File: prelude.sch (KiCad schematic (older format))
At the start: 1 part

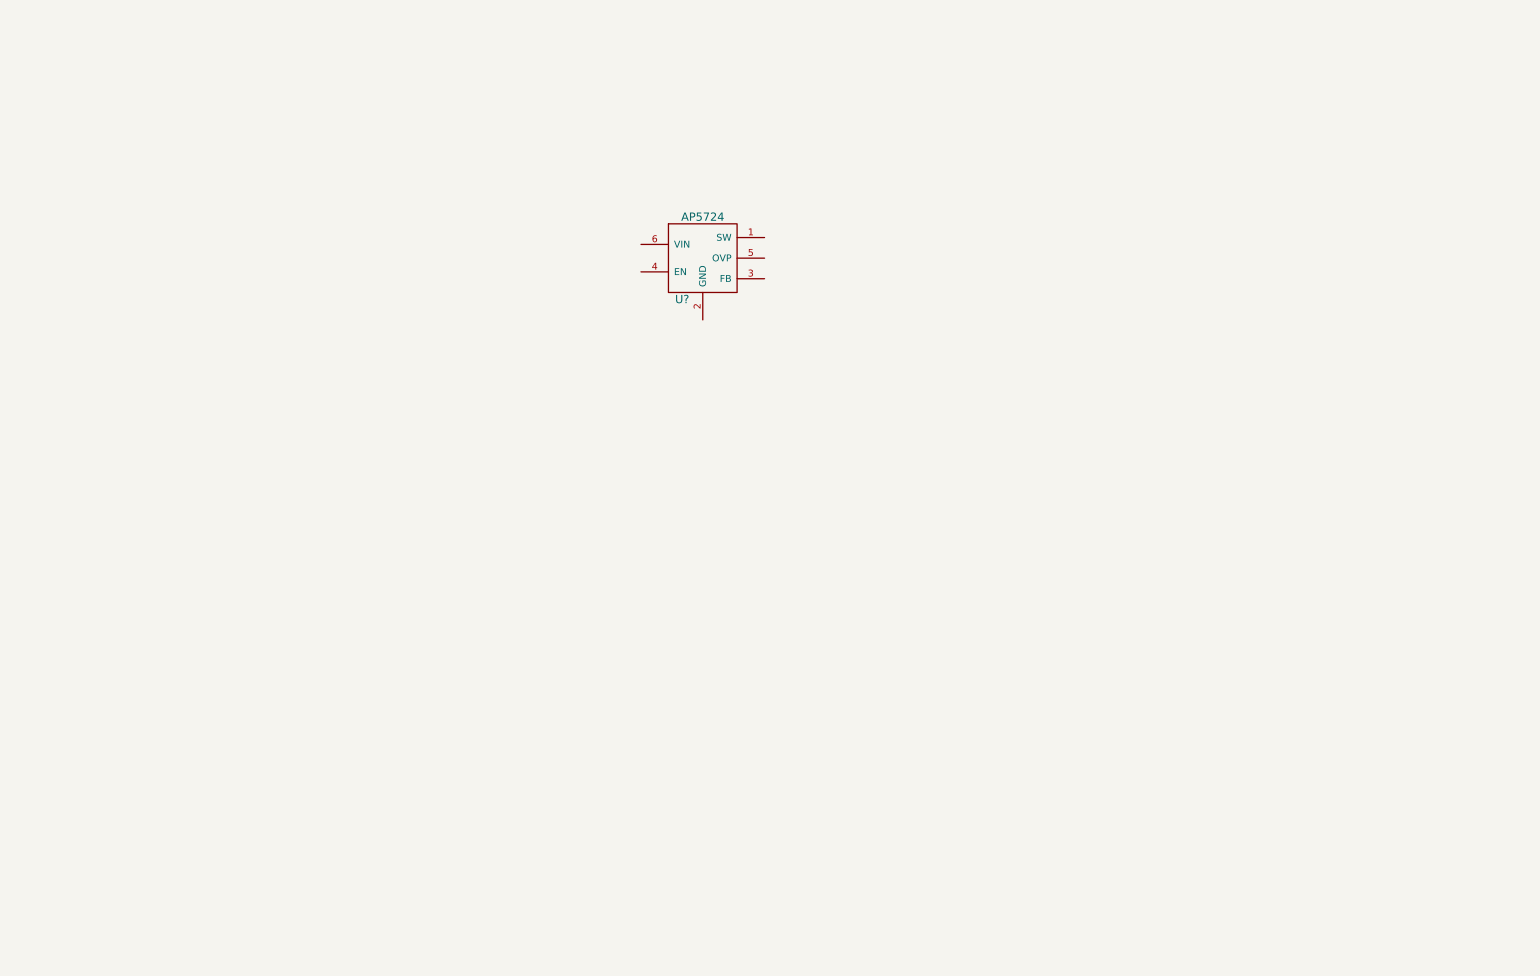
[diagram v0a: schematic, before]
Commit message: Adds MCU and 50 pin connector to schematic
Adds STM32F103RETx to schematic
Adds STM32 library to project
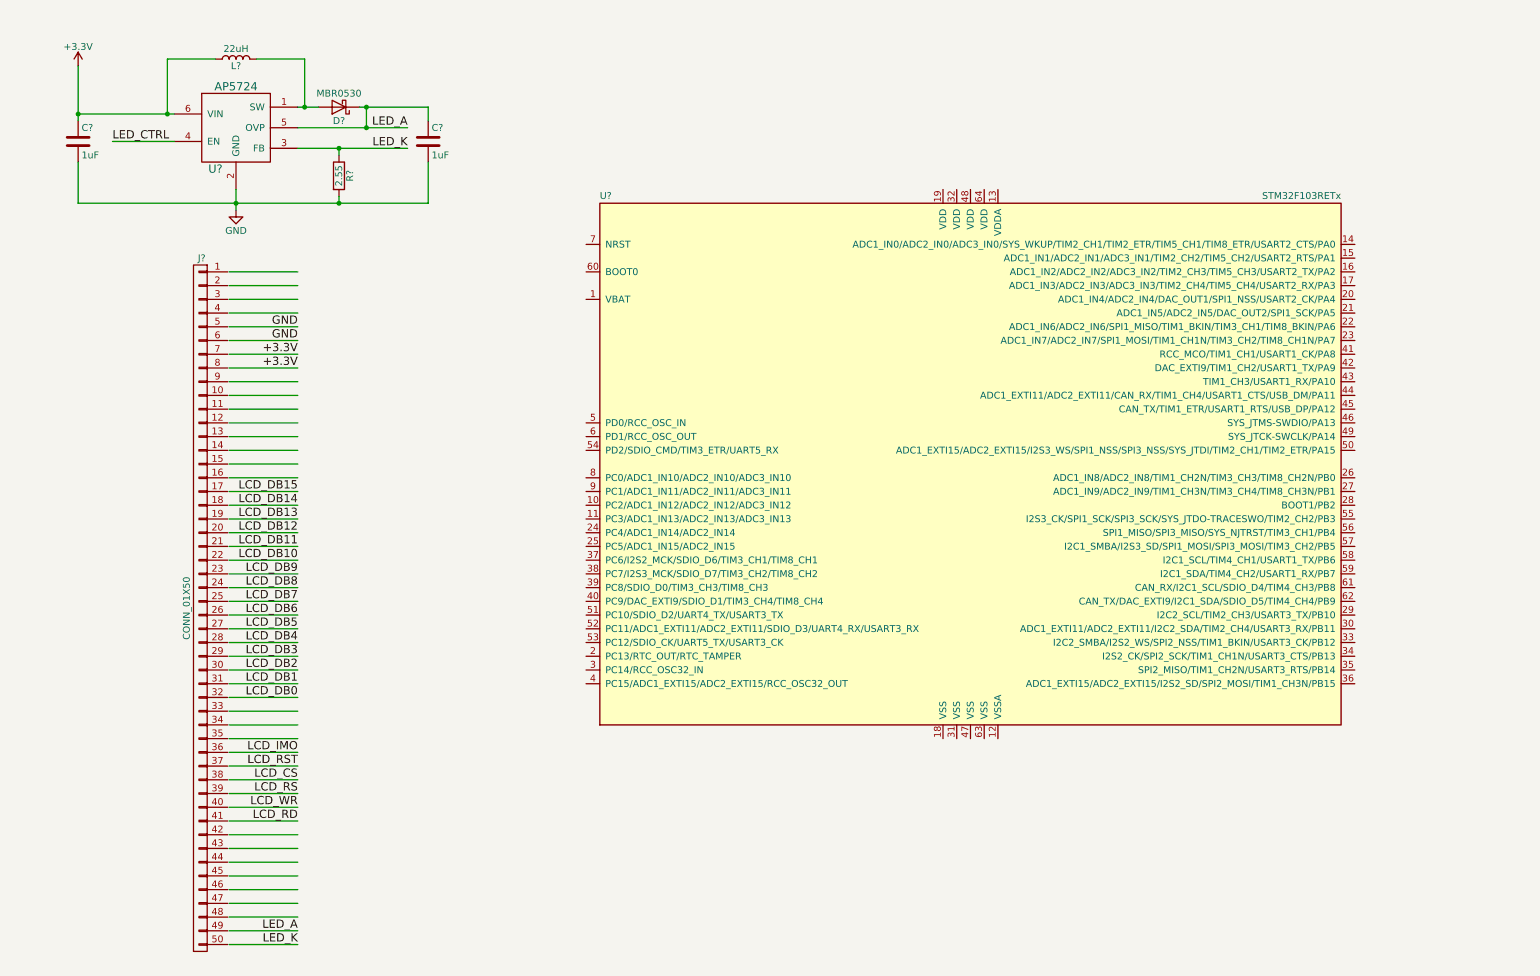
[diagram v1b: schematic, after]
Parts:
- added C? (x2): 1uF, symbol C
- added D?: MBR0530, symbol D_Schottky
- added J?: CONN_01X50, symbol CONN_01X50
- added L?: 22uH, symbol L
- added R?: 2.55, symbol R
- added U?: STM32F103RETx, LQFP64, symbol STM32F103RETx
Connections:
- net labels added: +3.3V, GND, LCD_CS, LCD_DB0, LCD_DB1, LCD_DB10, LCD_DB11, LCD_DB12, LCD_DB13, LCD_DB14, LCD_DB15, LCD_DB2, LCD_DB3, LCD_DB4, LCD_DB5, LCD_DB6, LCD_DB7, LCD_DB8, LCD_DB9, LCD_IMO, LCD_RD, LCD_RS, LCD_RST, LCD_WR, LED_A, LED_CTRL, LED_K
- wire segments 0 -> 69
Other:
- moved on the sheet: U?

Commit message: Adds main 3.3 power supply based on LM3671MF
Removed and added back 50-in connector, after fixing grid alignment
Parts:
- removed J?: CONN_01X50, symbol CONN_01X50
- added C?: 10uF, symbol C
- added C?: C, symbol C
- added D?: LED, symbol LED
- added F?: Polyfuse, symbol Polyfuse
- added J?: USB_OTG, symbol USB_OTG
- added J?: CONN_01X50, symbol CONN_01X50
- added L?: L, symbol L
- added R?: 330, symbol R
- added U?: LM3671MF-3.3, SOT95P284X122-5N, symbol LM3671MF-3.3
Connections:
- net labels added: +3V3, VCC
- wire segments 69 -> 84
- no-connect marks 0 -> 22
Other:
- moved on the sheet: C?, D?, L?, R?, U?

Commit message: Updates USB connector to to USB C
Added necessary connections and resistors (5.1K pulldown) to allow for device enumeration
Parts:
- removed J?: USB_OTG, symbol USB_OTG
- added J?: USB_C, symbol USB_C
- added R? (x2): 5K1, symbol R
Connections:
- net labels added: D+, D-, VBUS
- wire segments 84 -> 98
- no-connect marks 22 -> 32
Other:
- moved on the sheet: C?, D?, F?, L?, R?, U?

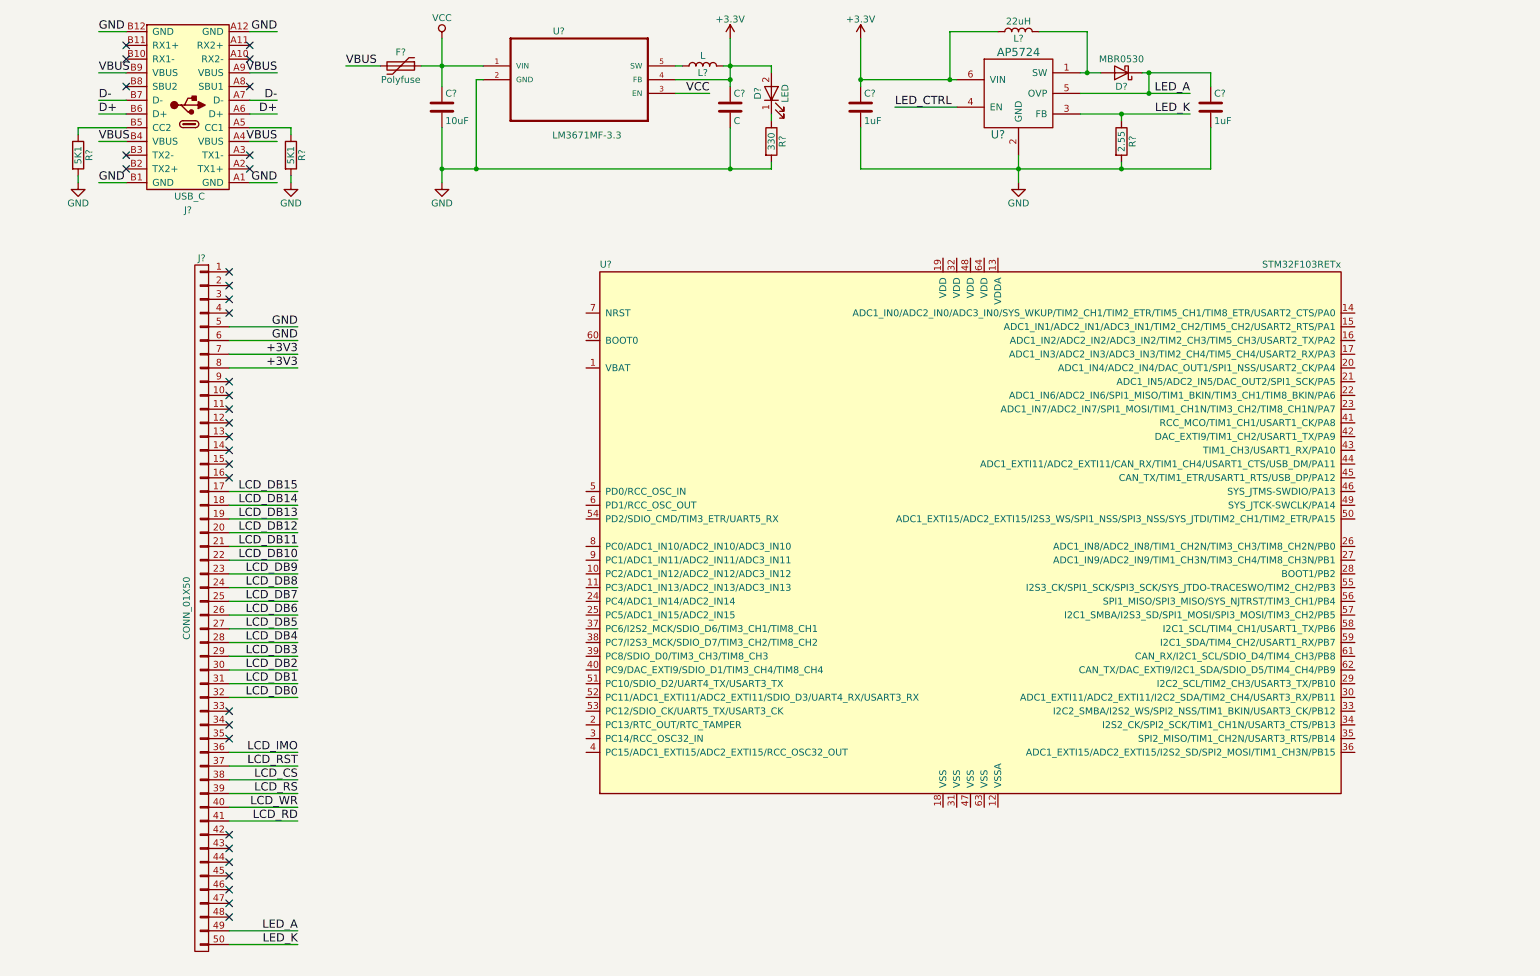
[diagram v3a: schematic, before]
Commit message: Updates schematic and project
Adds passives and wires to MCU
Adds switches library to project
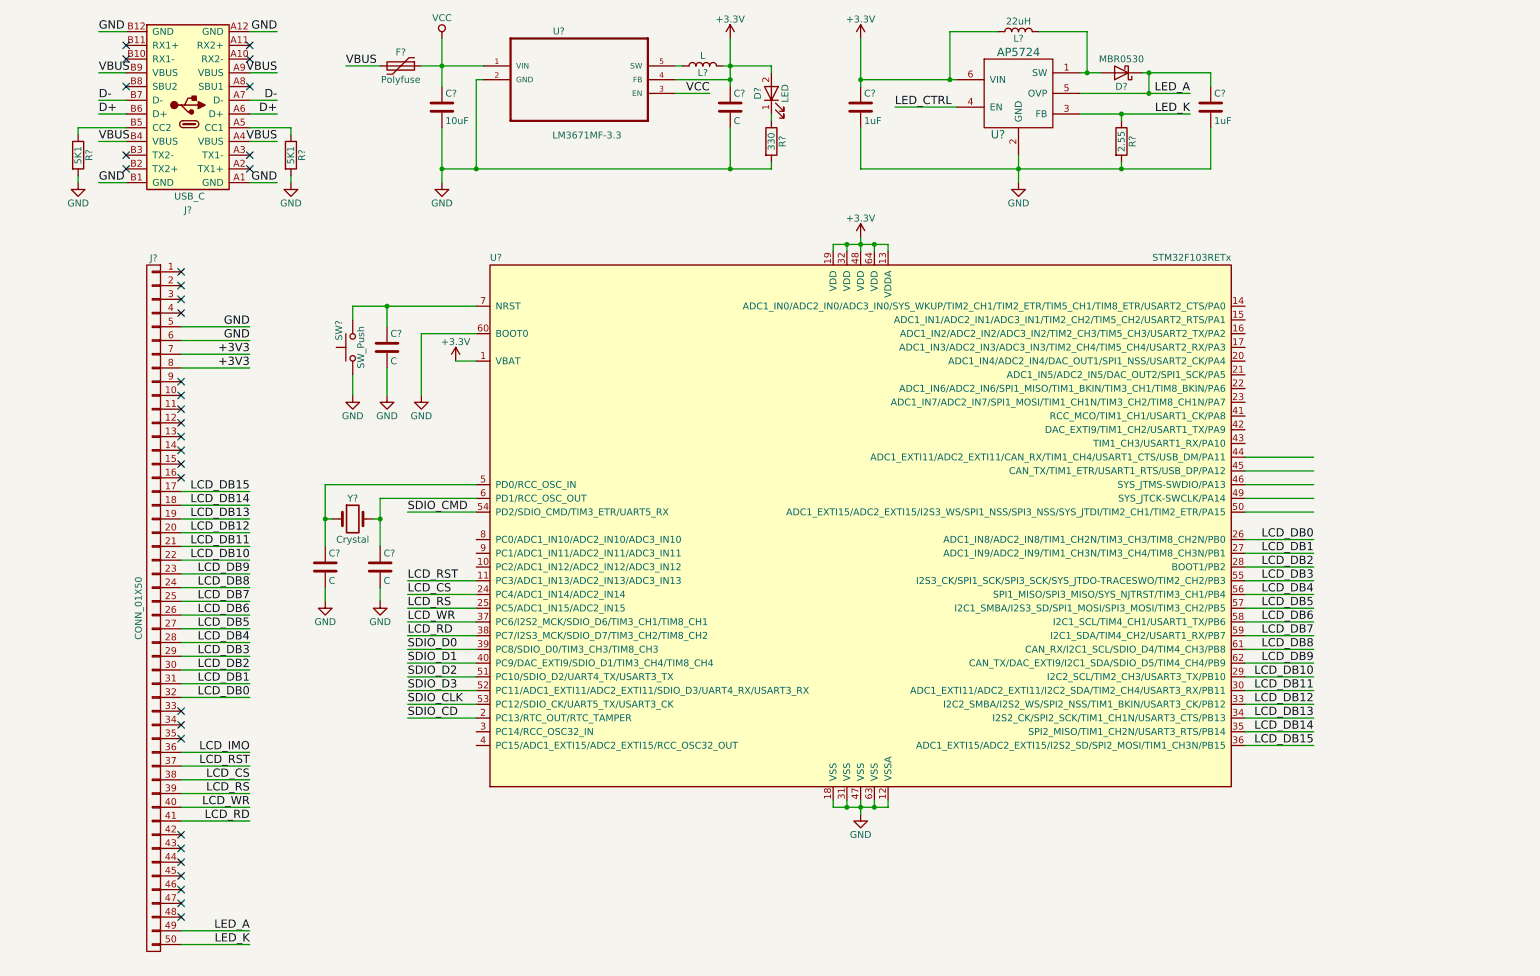
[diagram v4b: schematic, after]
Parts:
- added C? (x3): C, symbol C
- added SW?: SW_Push, symbol SW_Push
- added Y?: Crystal, symbol Crystal
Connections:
- net +3V3: now also U?.1 (VBAT), U?.13 (VDDA), U?.19 (VDD), U?.32 (VDD), U?.48 (VDD), U?.64 (VDD)
- net GND: now also U?.12 (VSSA), U?.18 (VSS), U?.31 (VSS), U?.47 (VSS), U?.60 (BOOT0), U?.63 (VSS), C?.2, C?.2, C?.2, SW?.1
- net LCD_CS: now also U?.24 (PC4/ADC1_IN14/ADC2_IN14)
- net LCD_DB0: now also U?.26 (ADC1_IN8/ADC2_IN8/TIM1_CH2N/TIM3_CH3/TIM8_CH2N/PB0)
- net LCD_DB1: now also U?.27 (ADC1_IN9/ADC2_IN9/TIM1_CH3N/TIM3_CH4/TIM8_CH3N/PB1)
- net LCD_DB10: now also U?.29 (I2C2_SCL/TIM2_CH3/USART3_TX/PB10)
- net LCD_DB11: now also U?.30 (ADC1_EXTI11/ADC2_EXTI11/I2C2_SDA/TIM2_CH4/USART3_RX/PB11)
- net LCD_DB12: now also U?.33 (I2C2_SMBA/I2S2_WS/SPI2_NSS/TIM1_BKIN/USART3_CK/PB12)
- net LCD_DB13: now also U?.34 (I2S2_CK/SPI2_SCK/TIM1_CH1N/USART3_CTS/PB13)
- net LCD_DB14: now also U?.35 (SPI2_MISO/TIM1_CH2N/USART3_RTS/PB14)
- net LCD_DB15: now also U?.36 (ADC1_EXTI15/ADC2_EXTI15/I2S2_SD/SPI2_MOSI/TIM1_CH3N/PB15)
- net LCD_DB2: now also U?.28 (BOOT1/PB2)
- net LCD_DB3: now also U?.55 (I2S3_CK/SPI1_SCK/SPI3_SCK/SYS_JTDO-TRACESWO/TIM2_CH2/PB3)
- net LCD_DB4: now also U?.56 (SPI1_MISO/SPI3_MISO/SYS_NJTRST/TIM3_CH1/PB4)
- net LCD_DB5: now also U?.57 (I2C1_SMBA/I2S3_SD/SPI1_MOSI/SPI3_MOSI/TIM3_CH2/PB5)
- net LCD_DB6: now also U?.58 (I2C1_SCL/TIM4_CH1/USART1_TX/PB6)
- net LCD_DB7: now also U?.59 (I2C1_SDA/TIM4_CH2/USART1_RX/PB7)
- net LCD_DB8: now also U?.61 (CAN_RX/I2C1_SCL/SDIO_D4/TIM4_CH3/PB8)
- net LCD_DB9: now also U?.62 (CAN_TX/DAC_EXTI9/I2C1_SDA/SDIO_D5/TIM4_CH4/PB9)
- net LCD_RD: now also U?.38 (PC7/I2S3_MCK/SDIO_D7/TIM3_CH2/TIM8_CH2)
- net LCD_RS: now also U?.25 (PC5/ADC1_IN15/ADC2_IN15)
- net LCD_RST: now also U?.11 (PC3/ADC1_IN13/ADC2_IN13/ADC3_IN13)
- net LCD_WR: now also U?.37 (PC6/I2S2_MCK/SDIO_D6/TIM3_CH1/TIM8_CH1)
- net SDIO_CD: now reaches U?.2 (PC13/RTC_OUT/RTC_TAMPER)
- net SDIO_D0: now reaches U?.39 (PC8/SDIO_D0/TIM3_CH3/TIM8_CH3)
- net SDIO_D1: now reaches U?.40 (PC9/DAC_EXTI9/SDIO_D1/TIM3_CH4/TIM8_CH4)
- net at U?.5 (PD0/RCC_OSC_IN): now also C?.1, Y?.1
- net SDIO_D2: now reaches U?.51 (PC10/SDIO_D2/UART4_TX/USART3_TX)
- net SDIO_D3: now reaches U?.52 (PC11/ADC1_EXTI11/ADC2_EXTI11/SDIO_D3/UART4_RX/USART3_RX)
- net SDIO_CLK: now reaches U?.53 (PC12/SDIO_CK/UART5_TX/USART3_CK)
- net SDIO_CMD: now reaches U?.54 (PD2/SDIO_CMD/TIM3_ETR/UART5_RX)
- net at U?.6 (PD1/RCC_OSC_OUT): now also C?.1, Y?.2
- net at U?.7 (NRST): now also C?.1, SW?.2
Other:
- moved on the sheet: J?, U?

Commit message: Several updates to schematic
Adds decoupling capacitors
Adds debug connector
Adds values to several components
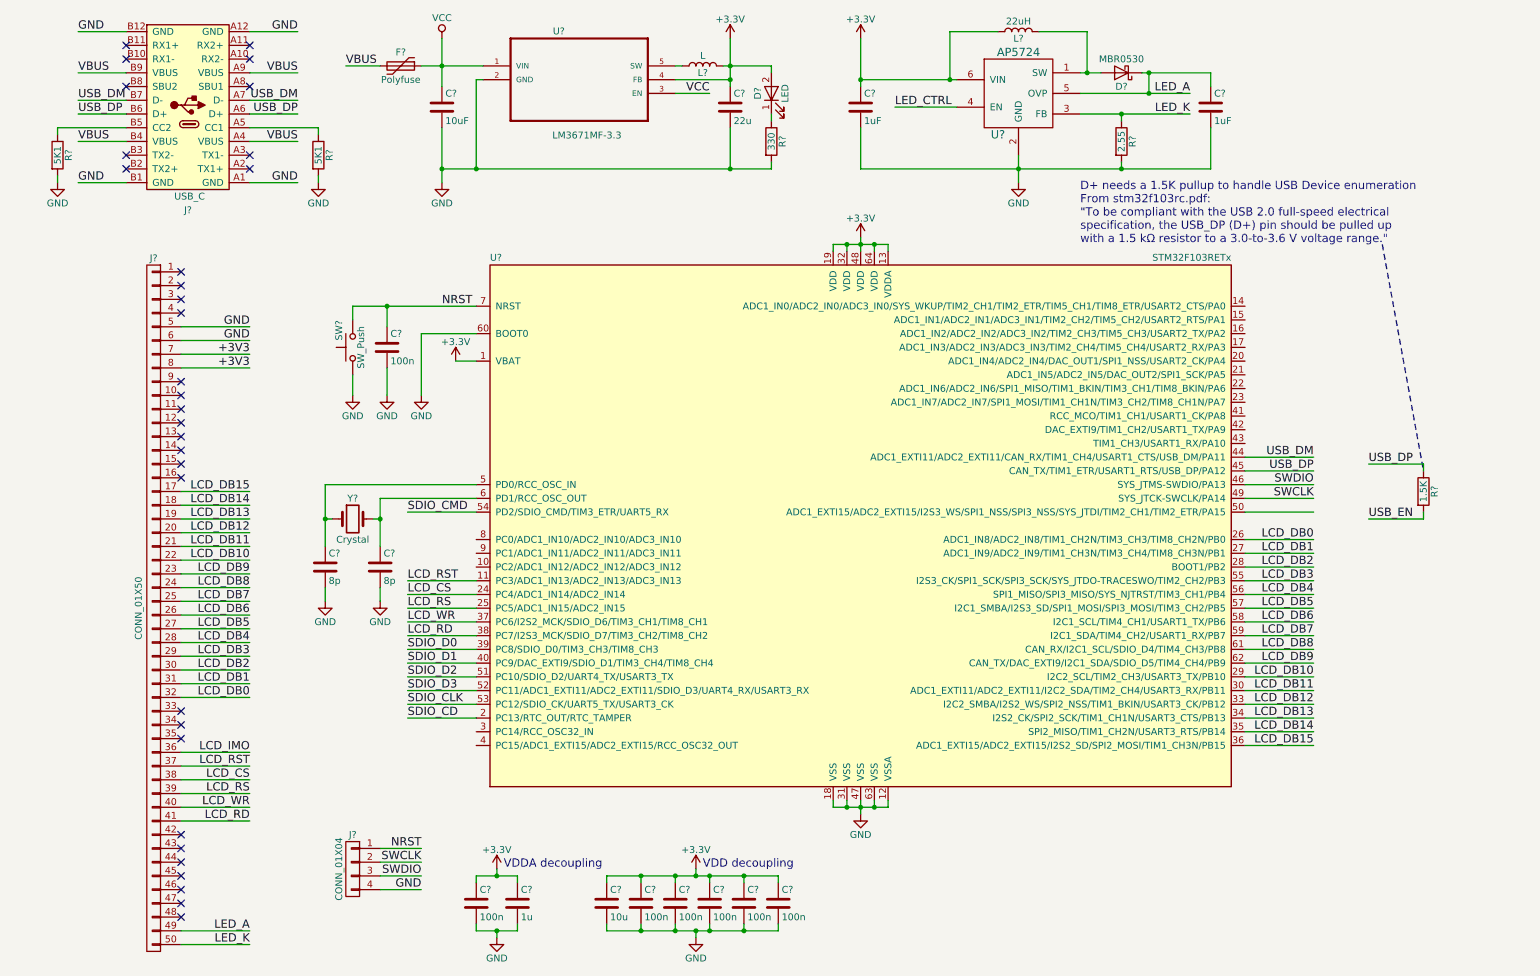
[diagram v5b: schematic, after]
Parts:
- added C? (x6): 100n, symbol C
- added C?: 1u, symbol C
- added C?: 10u, symbol C
- added J?: CONN_01X04, symbol CONN_01X04
- added R?: 1.5K, symbol R
- C?: value C -> 22u
- C?: value C -> 100n
- C? (x2): value C -> 8p
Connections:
- net D+ is gone; now on net USB_DP: J?.A6 (D+), J?.B6 (D+)
- net D- is gone; now on net USB_DM: J?.A7 (D-), J?.B7 (D-)
- net +3V3: now also C?.1, C?.1, C?.1, C?.1, C?.1, C?.1, C?.1, C?.1
- net GND: now also C?.2, C?.2, C?.2, C?.2, C?.2, C?.2, C?.2, C?.2, J?.4 (P4)
- net USB_DM: now reaches U?.44 (ADC1_EXTI11/ADC2_EXTI11/CAN_RX/TIM1_CH4/USART1_CTS/USB_DM/PA11)
- net USB_DP: now reaches U?.45 (CAN_TX/TIM1_ETR/USART1_RTS/USB_DP/PA12)
- net USB_DP: now also R?.1
- net SWDIO: now reaches U?.46 (SYS_JTMS-SWDIO/PA13)
- net SWDIO: now also J?.3 (P3)
- net SWCLK: now reaches U?.49 (SYS_JTCK-SWCLK/PA14)
- net SWCLK: now also J?.2 (P2)
- net NRST: now reaches C?.1, SW?.2, U?.7 (NRST)
- net NRST: now also J?.1 (P1)
- new net USB_EN: R?.2
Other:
- note added: "D+ needs a 1.5K pullup to handle USB Device enumeration\nFrom stm32f103rc.pdf:\n"To be compliant with the USB 2.0 full-speed electrical\nspecification, the USB_DP (D+) pin should be pulled up\nwith a 1.5 kΩ resistor to a 3.0-to-3.6 V voltage range.""
- note added: "VDD decoupling"
- note added: "VDDA decoupling"
- moved on the sheet: R?
